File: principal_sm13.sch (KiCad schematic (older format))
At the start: 0 parts

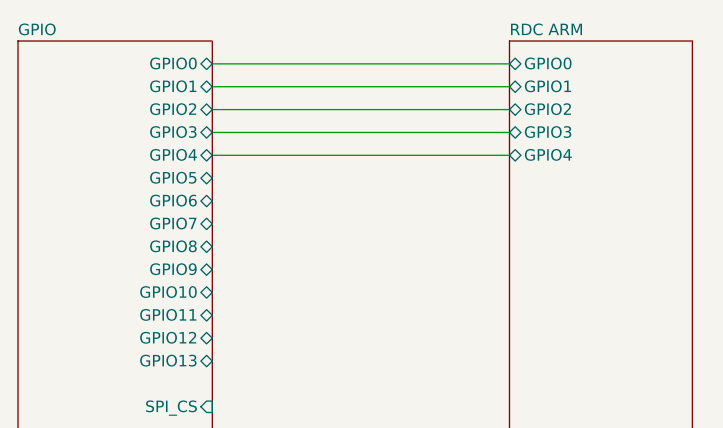
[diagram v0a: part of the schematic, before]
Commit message: resolución fijada en 16 bits y modo configuración fijado
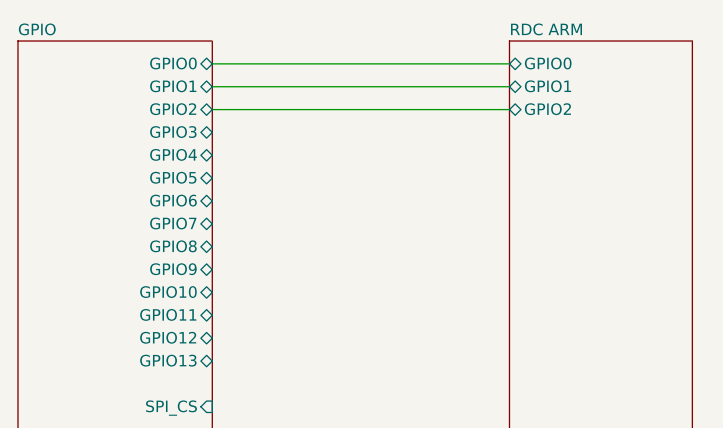
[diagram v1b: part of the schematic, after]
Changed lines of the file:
@@
-$EndSheet
-$Sheet
-S 3950 1100 800  2300
-U 5EF45E27
-F0 "RDC ARM" 50
-F1 "RDC_ARM.sch" 50
-F2 "MISO" B L 3950 3150 50
-F3 "MOSI" B L 3950 3000 50
-F4 "spiSCK" B L 3950 2850 50
-F5 "GPIO3" B L 3950 1500 50
-F6 "GPIO2" B L 3950 1400 50
-F7 "GPIO0" B L 3950 1200 50
-F8 "GPIO1" B L 3950 1300 50
-F9 "GPIO4" B L 3950 1600 50
 $EndSheet
 $Sheet
@@
 	2650 1300 3950 1300
 Wire Wire Line
-	2650 1400 3950 1400
-Wire Wire Line
-	2650 1500 3950 1500
-Wire Wire Line
 	2650 2850 3950 2850
 Wire Wire Line
@@
 	2650 3150 3950 3150
 Wire Wire Line
-	2650 1600 3950 1600
+	2650 1400 3950 1400
+$Sheet
+S 3950 1100 800  2300
+U 5EF45E27
+F0 "RDC ARM" 50
+F1 "RDC_ARM.sch" 50
+F2 "MISO" B L 3950 3150 50
+F3 "MOSI" B L 3950 3000 50
+F4 "spiSCK" B L 3950 2850 50
+F5 "GPIO2" B L 3950 1400 50
+F6 "GPIO0" B L 3950 1200 50
+F7 "GPIO1" B L 3950 1300 50
+$EndSheet
 $EndSCHEMATC

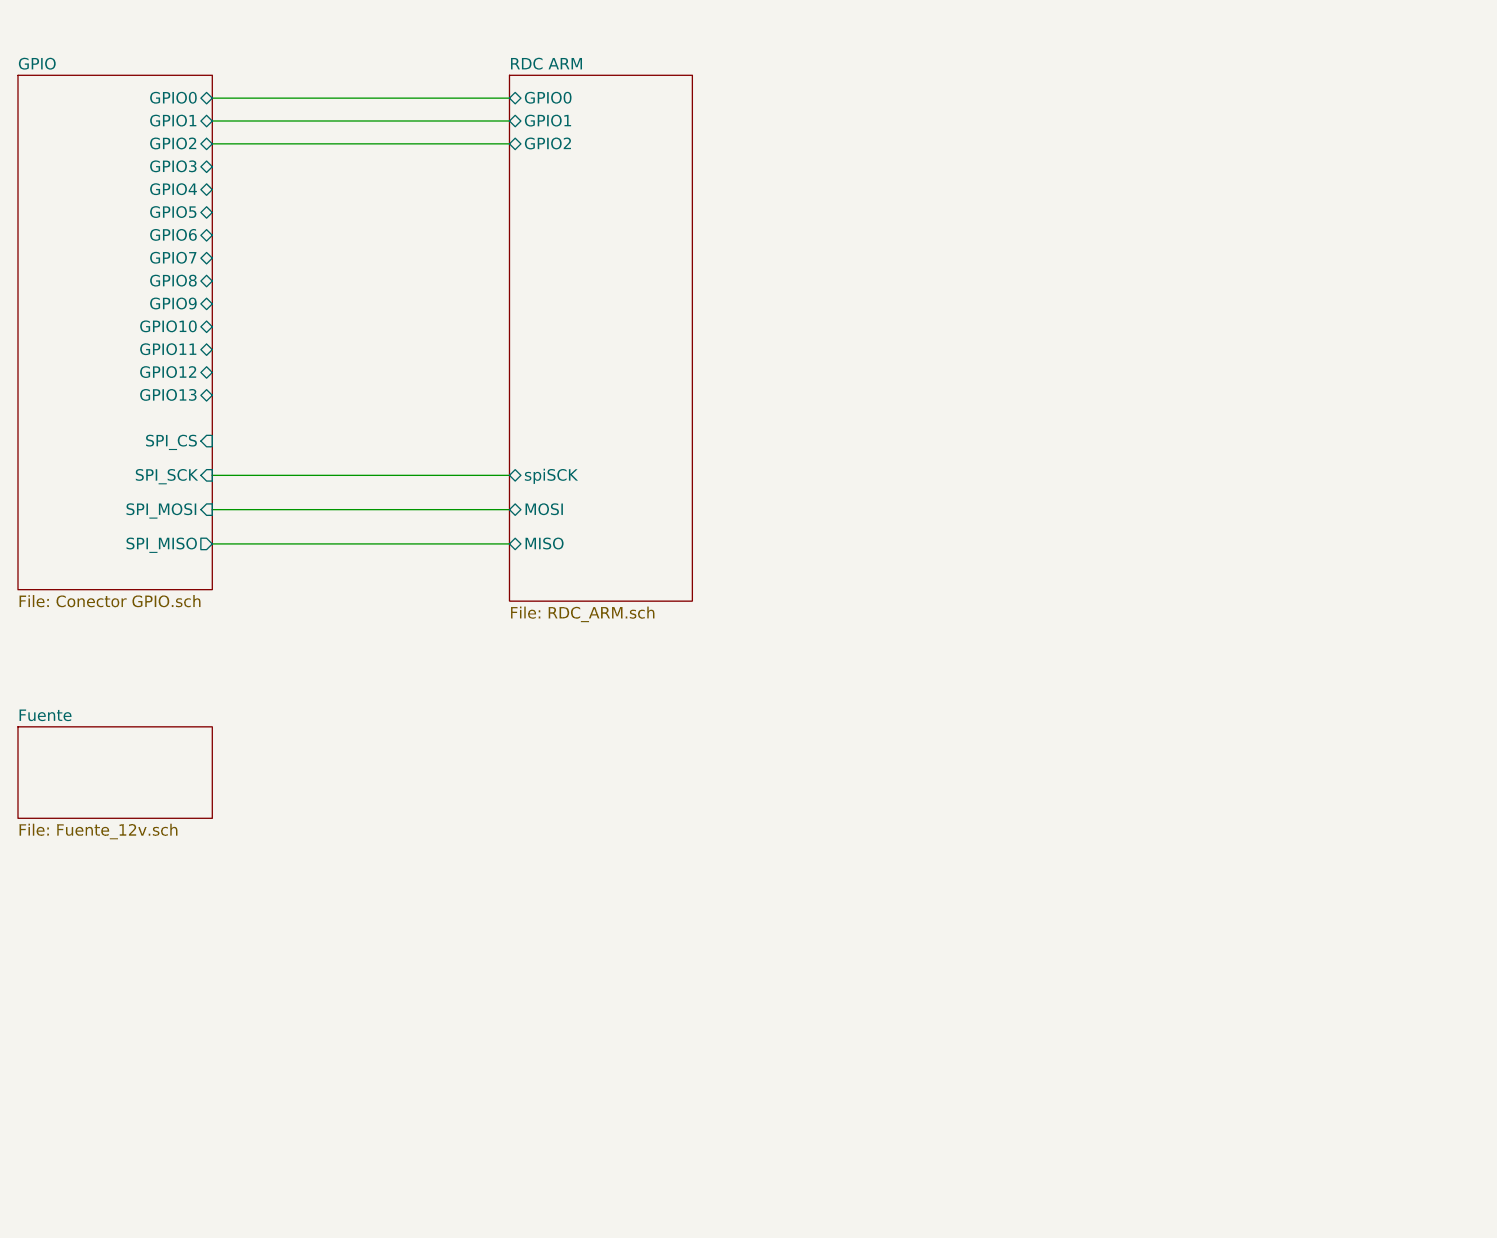
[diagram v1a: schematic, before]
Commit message: agregado el segundo RDC, leds conectados a +5v, asignados footprints
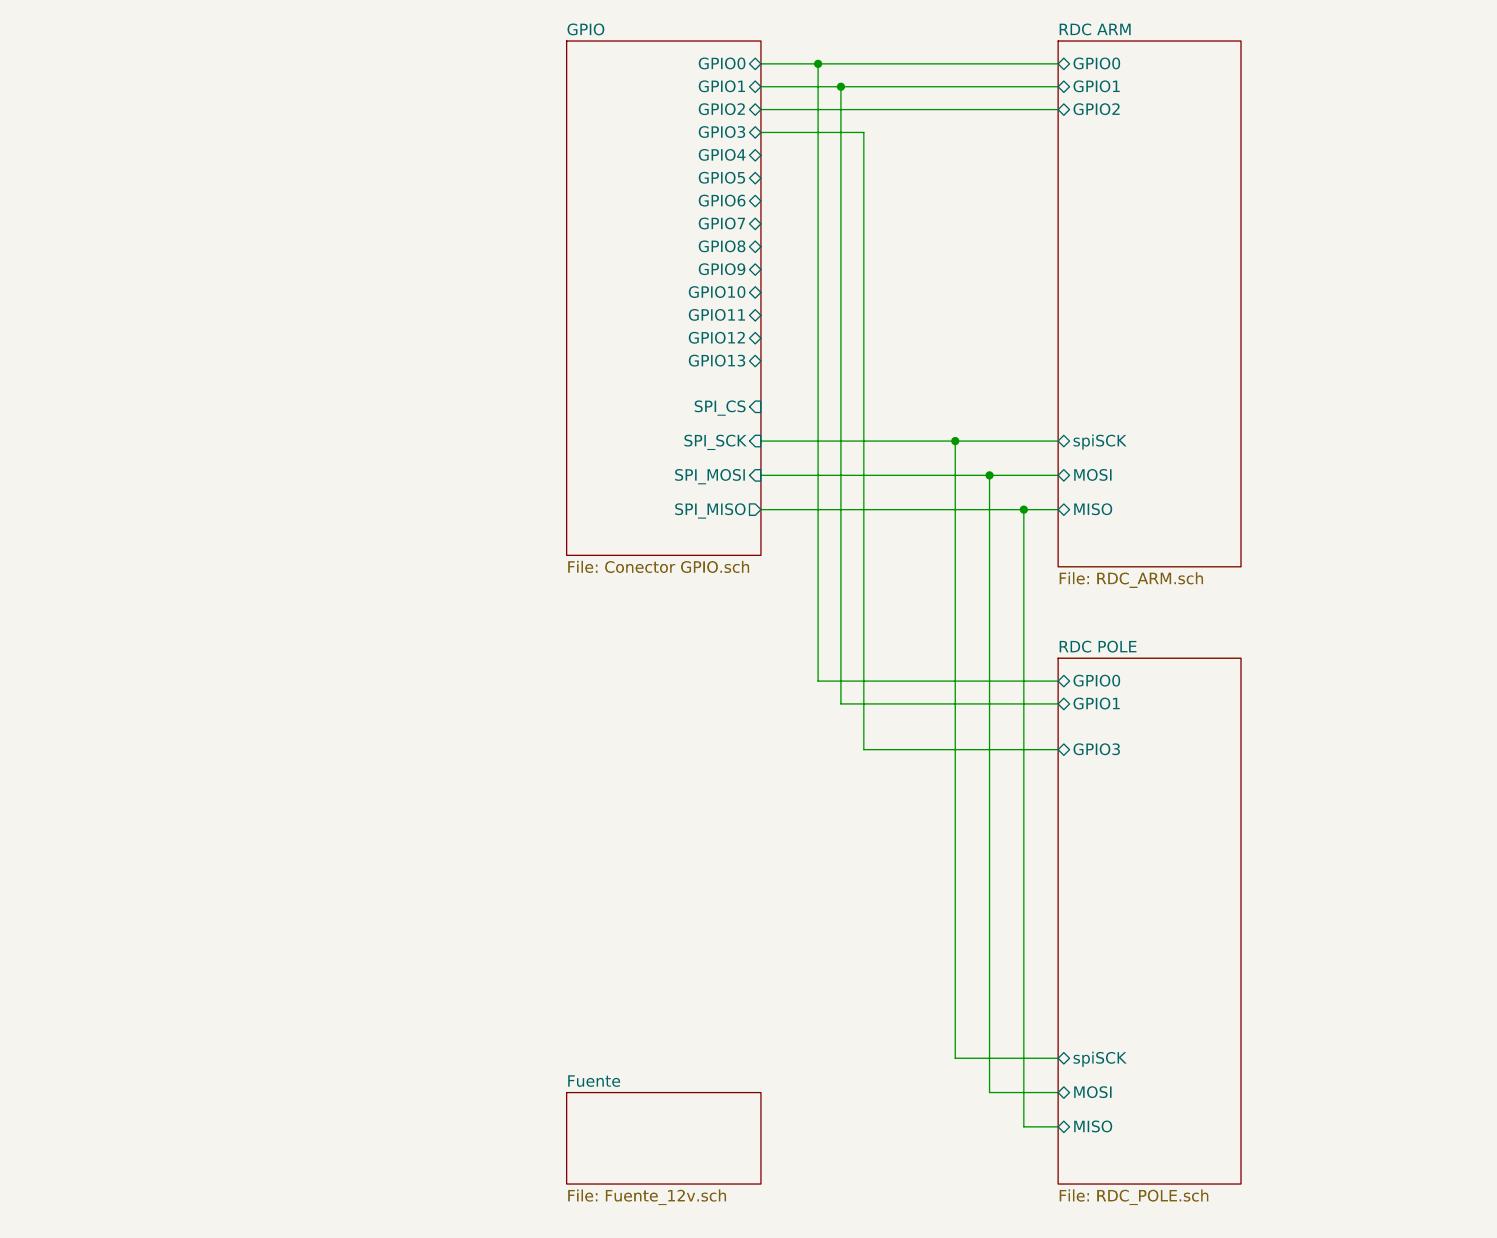
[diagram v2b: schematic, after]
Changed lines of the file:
@@
 $Descr A4 11693 8268
 encoding utf-8
-Sheet 1 4
+Sheet 1 5
 Title "RDC"
 Date "2020-06-22"
@@
 $EndDescr
 $Sheet
-S 1800 3950 850  400
+S 4200 950  850  2250
+U 5EF2A268
+F0 "GPIO" 50
+F1 "Conector GPIO.sch" 50
+F2 "GPIO0" B R 5050 1050 50
+F3 "GPIO2" B R 5050 1250 50
+F4 "GPIO4" B R 5050 1450 50
+F5 "GPIO6" B R 5050 1650 50
+F6 "GPIO8" B R 5050 1850 50
+F7 "GPIO10" B R 5050 2050 50
+F8 "GPIO12" B R 5050 2250 50
+F9 "GPIO1" B R 5050 1150 50
+F10 "GPIO3" B R 5050 1350 50
+F11 "GPIO5" B R 5050 1550 50
+F12 "GPIO7" B R 5050 1750 50
+F13 "GPIO9" B R 5050 1950 50
+F14 "GPIO11" B R 5050 2150 50
+F15 "GPIO13" B R 5050 2350 50
+F16 "SPI_MISO" O R 5050 3000 50
+F17 "SPI_MOSI" I R 5050 2850 50
+F18 "SPI_SCK" I R 5050 2700 50
+F19 "SPI_CS" I R 5050 2550 50
+$EndSheet
+Wire Wire Line
+	5050 1050 5300 1050
+Wire Wire Line
+	5050 1150 5400 1150
+Wire Wire Line
+	5050 2700 5900 2700
+Wire Wire Line
+	5050 2850 6050 2850
+Wire Wire Line
+	5050 1250 6350 1250
+$Sheet
+S 6350 950  800  2300
+U 5EF45E27
+F0 "RDC ARM" 50
+F1 "RDC_ARM.sch" 50
+F2 "MISO" B L 6350 3000 50
+F3 "MOSI" B L 6350 2850 50
+F4 "spiSCK" B L 6350 2700 50
+F5 "GPIO2" B L 6350 1250 50
+F6 "GPIO0" B L 6350 1050 50
+F7 "GPIO1" B L 6350 1150 50
+$EndSheet
+Wire Wire Line
+	5050 3000 6200 3000
+Wire Wire Line
+	5900 2700 5900 5400
+Wire Wire Line
+	6050 2850 6050 5550
+Wire Wire Line
+	6200 3000 6200 5700
+Connection ~ 5900 2700
+Connection ~ 6050 2850
+Connection ~ 6200 3000
+Wire Wire Line
+	5900 2700 6350 2700
+Wire Wire Line
+	6050 2850 6350 2850
+Wire Wire Line
+	6200 3000 6350 3000
+Wire Wire Line
+	5900 5400 6350 5400
+Wire Wire Line
+	6050 5550 6350 5550
+Wire Wire Line
+	6200 5700 6350 5700
+Wire Wire Line
+	5300 1050 5300 3750
+Connection ~ 5300 1050
+Wire Wire Line
+	5300 1050 6350 1050
+Wire Wire Line
+	5300 3750 6350 3750
+Wire Wire Line
+	5400 1150 5400 3850
+Connection ~ 5400 1150
+Wire Wire Line
+	5400 1150 6350 1150
+Wire Wire Line
+	5400 3850 6350 3850
+$Sheet
+S 6350 3650 800  2300
+U 5F077C82
+F0 "RDC POLE" 50
+F1 "RDC_POLE.sch" 50
+F2 "MISO" B L 6350 5700 50
+F3 "MOSI" B L 6350 5550 50
+F4 "spiSCK" B L 6350 5400 50
+F5 "GPIO0" B L 6350 3750 50
+F6 "GPIO1" B L 6350 3850 50
+F7 "GPIO3" B L 6350 4050 50
+$EndSheet
+Wire Wire Line
+	5050 1350 5500 1350
+Wire Wire Line
+	5500 1350 5500 4050
+Wire Wire Line
+	5500 4050 6350 4050
+$Sheet
+S 4200 5550 850  400
 U 5EF34214
 F0 "Fuente" 50
 F1 "Fuente_12v.sch" 50
 $EndSheet
-$Sheet
-S 1800 1100 850  2250
-U 5EF2A268
-F0 "GPIO" 50
-F1 "Conector GPIO.sch" 50
-F2 "GPIO0" B R 2650 1200 50
-F3 "GPIO2" B R 2650 1400 50
-F4 "GPIO4" B R 2650 1600 50
-F5 "GPIO6" B R 2650 1800 50
-F6 "GPIO8" B R 2650 2000 50
-F7 "GPIO10" B R 2650 2200 50
-F8 "GPIO12" B R 2650 2400 50
-F9 "GPIO1" B R 2650 1300 50
-F10 "GPIO3" B R 2650 1500 50
-F11 "GPIO5" B R 2650 1700 50
-F12 "GPIO7" B R 2650 1900 50
-F13 "GPIO9" B R 2650 2100 50
-F14 "GPIO11" B R 2650 2300 50
-F15 "GPIO13" B R 2650 2500 50
-F16 "SPI_MISO" O R 2650 3150 50
-F17 "SPI_MOSI" I R 2650 3000 50
-F18 "SPI_SCK" I R 2650 2850 50
-F19 "SPI_CS" I R 2650 2700 50
-$EndSheet
-Wire Wire Line
-	2650 1200 3950 1200
-Wire Wire Line
-	2650 1300 3950 1300
-Wire Wire Line
-	2650 2850 3950 2850
-Wire Wire Line
-	2650 3000 3950 3000
-Wire Wire Line
-	2650 3150 3950 3150
-Wire Wire Line
-	2650 1400 3950 1400
-$Sheet
-S 3950 1100 800  2300
-U 5EF45E27
-F0 "RDC ARM" 50
-F1 "RDC_ARM.sch" 50
-F2 "MISO" B L 3950 3150 50
-F3 "MOSI" B L 3950 3000 50
-F4 "spiSCK" B L 3950 2850 50
-F5 "GPIO2" B L 3950 1400 50
-F6 "GPIO0" B L 3950 1200 50
-F7 "GPIO1" B L 3950 1300 50
-$EndSheet
 $EndSCHEMATC

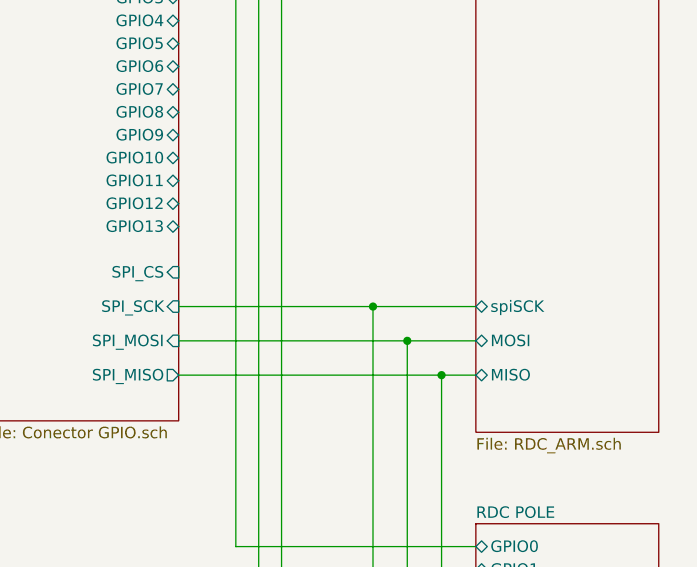
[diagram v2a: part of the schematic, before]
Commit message: agregados test points parara comunicacion SPI, ruteado, 28 vias
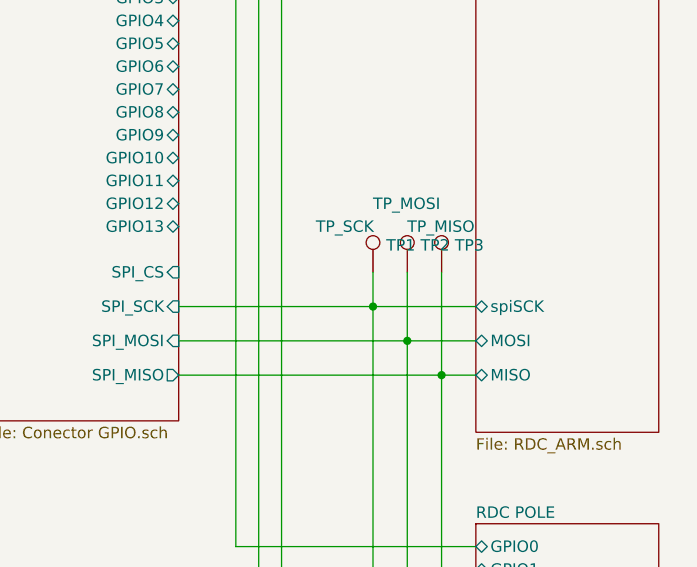
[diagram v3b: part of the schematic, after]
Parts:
- added TP1: TP_SCK, TestPoint:TestPoint_THTPad_1.0x1.0mm_Drill0.5mm, symbol Connector:TestPoint
- added TP2: TP_MOSI, TestPoint:TestPoint_THTPad_1.0x1.0mm_Drill0.5mm, symbol Connector:TestPoint
- added TP3: TP_MISO, TestPoint:TestPoint_THTPad_1.0x1.0mm_Drill0.5mm, symbol Connector:TestPoint
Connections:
- net GPIO/SPI_MISO: now also TP3.1
- net GPIO/SPI_MOSI: now also TP2.1
- net GPIO/SPI_SCK: now also TP1.1
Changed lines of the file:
@@
 F1 "Fuente_12v.sch" 50
 $EndSheet
+$Comp
+L Connector:TestPoint TP1
+U 1 1 5F11CC37
+P 5900 2550
+F 0 "TP1" H 5958 2668 50  0000 L CNN
+F 1 "TP_SCK" H 5650 2750 50  0000 L CNN
+F 2 "TestPoint:TestPoint_THTPad_1.0x1.0mm_Drill0.5mm" H 6100 2550 50  0001 C CNN
+F 3 "~" H 6100 2550 50  0001 C CNN
+	1    5900 2550
+	1    0    0    -1
+$EndComp
+$Comp
+L Connector:TestPoint TP2
+U 1 1 5F11D1E5
+P 6050 2550
+F 0 "TP2" H 6108 2668 50  0000 L CNN
+F 1 "TP_MOSI" H 5900 2850 50  0000 L CNN
+F 2 "TestPoint:TestPoint_THTPad_1.0x1.0mm_Drill0.5mm" H 6250 2550 50  0001 C CNN
+F 3 "~" H 6250 2550 50  0001 C CNN
+	1    6050 2550
+	1    0    0    -1
+$EndComp
+$Comp
+L Connector:TestPoint TP3
+U 1 1 5F11D4A3
+P 6200 2550
+F 0 "TP3" H 6258 2668 50  0000 L CNN
+F 1 "TP_MISO" H 6050 2750 50  0000 L CNN
+F 2 "TestPoint:TestPoint_THTPad_1.0x1.0mm_Drill0.5mm" H 6400 2550 50  0001 C CNN
+F 3 "~" H 6400 2550 50  0001 C CNN
+	1    6200 2550
+	1    0    0    -1
+$EndComp
+Wire Wire Line
+	5900 2550 5900 2700
+Wire Wire Line
+	6050 2550 6050 2850
+Wire Wire Line
+	6200 2550 6200 3000
 $EndSCHEMATC
